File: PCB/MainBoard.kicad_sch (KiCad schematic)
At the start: 34 parts, among them J1 DM3AT-SF-PEJM5, J3 PROG, J5 Conn_01x03, J5 Conn_01x07, SW1 SW_Push, SW2 SW_Push, SW3 SW_Push, U1 ESP32-WROOM-32D, U3 MPU-6050, U8 GY-521

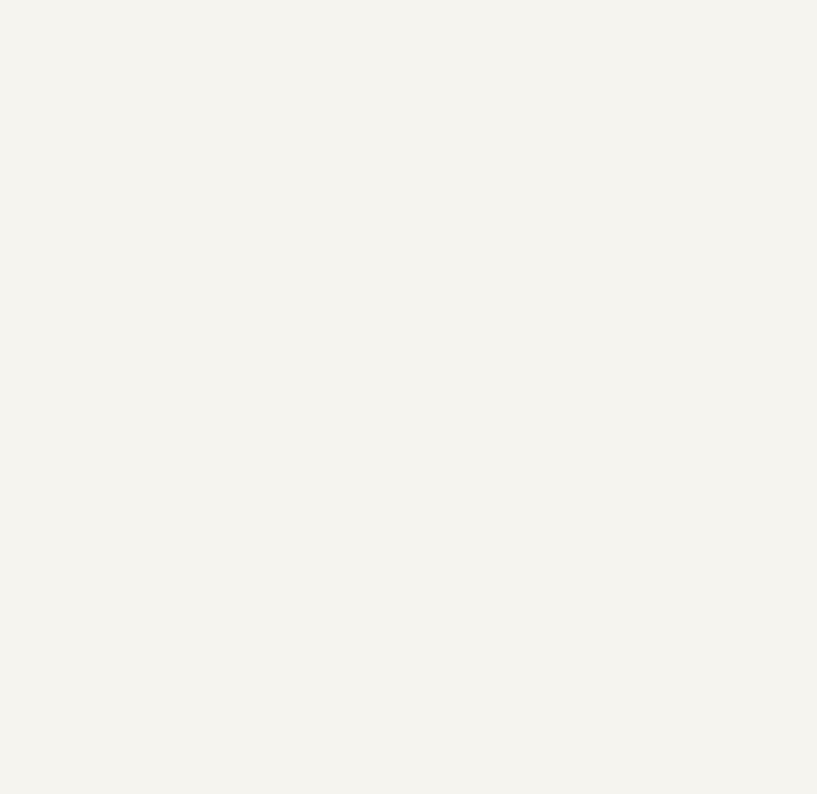
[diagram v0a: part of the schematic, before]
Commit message: Added RTC circuit
Signed-off-by: theloukou
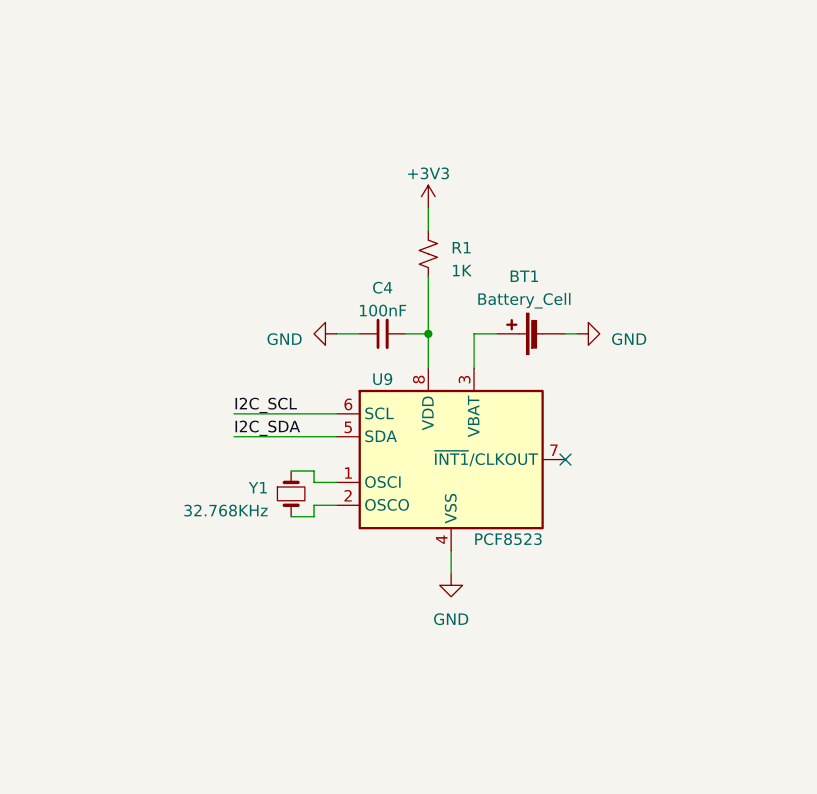
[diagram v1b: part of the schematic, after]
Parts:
- added BT1: Battery_Cell, Battery:BatteryHolder_Keystone_3000_1x12mm, symbol Device:Battery_Cell
- added C4: 100nF, Capacitor_SMD:C_0603_1608Metric, symbol Device:C_Small
- added R1: 1K, Resistor_SMD:R_0603_1608Metric, symbol Device:R_Small_US
- added U9: PCF8523, Package_SO:SOIC-8_3.9x4.9mm_P1.27mm, symbol Timer_RTC:PCF8523T
- added Y1: 32.768KHz, Crystal:Crystal_C38-LF_D3.0mm_L8.0mm_Horizontal, symbol Device:Crystal_Small
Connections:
- net +3V3: now also R1.1
- net GND: now also BT1.2 (-), C4.1, U9.4 (VSS)
- net I2C_SCL: now also U9.6 (SCL)
- net I2C_SDA: now also U9.5 (SDA)
- new net: C4.2, R1.2, U9.8 (VDD)
- new net: U9.1 (OSCI), Y1.1
- new net: U9.2 (OSCO), Y1.2
- new net: BT1.1 (+), U9.3 (VBAT)
- no-connect marks 19 -> 20

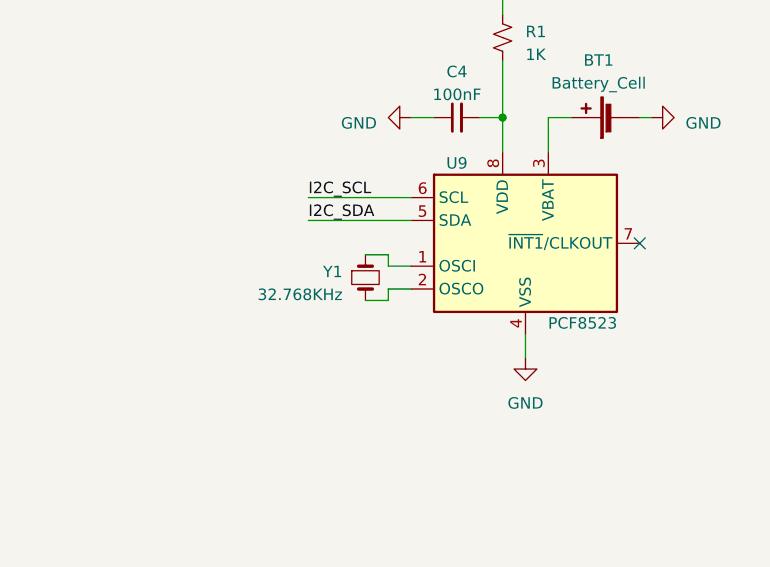
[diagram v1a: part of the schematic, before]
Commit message: Finalized RTC layout changes
Signed-off-by: theloukou
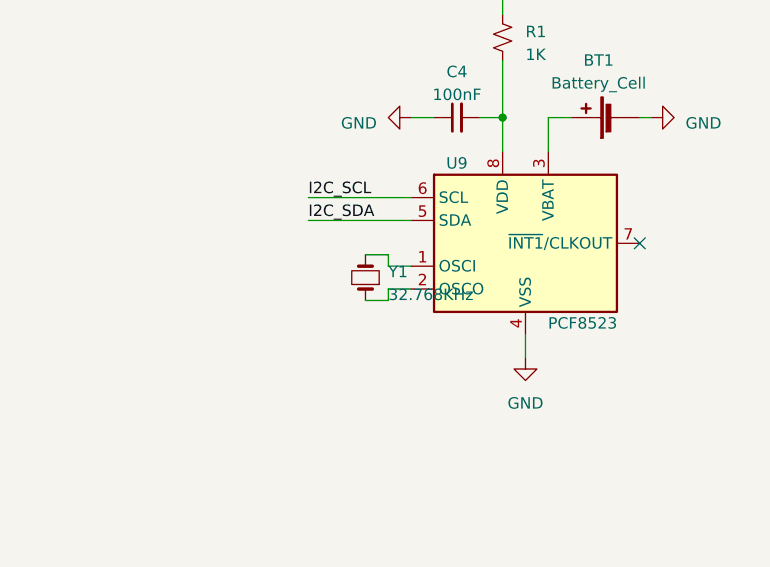
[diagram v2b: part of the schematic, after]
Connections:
- net at Y1.1: now also U9.2 (OSCO); no longer U9.1 (OSCI)
- net at Y1.2: now also U9.1 (OSCI); no longer U9.2 (OSCO)
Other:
- moved on the sheet: Y1
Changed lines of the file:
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@@
     )
   )
-  (symbol (lib_id "Device:Crystal_Small") (at 64.77 171.45 270) (unit 1)
+  (symbol (lib_id "Device:Crystal_Small") (at 64.77 171.45 90) (unit 1)
     (in_bom yes) (on_board yes) (dnp no) (fields_autoplaced)
-    (property "Reference" "Y1" (at 62.23 170.815 90)
+    (property "Reference" "Y1" (at 67.31 170.815 90)
       (effects (font (size 1.27 1.27)) (justify right))
     )
-    (property "Value" "32.768KHz" (at 62.23 173.355 90)
+    (property "Value" "32.768KHz" (at 67.31 173.355 90)
       (effects (font (size 1.27 1.27)) (justify right))
     )

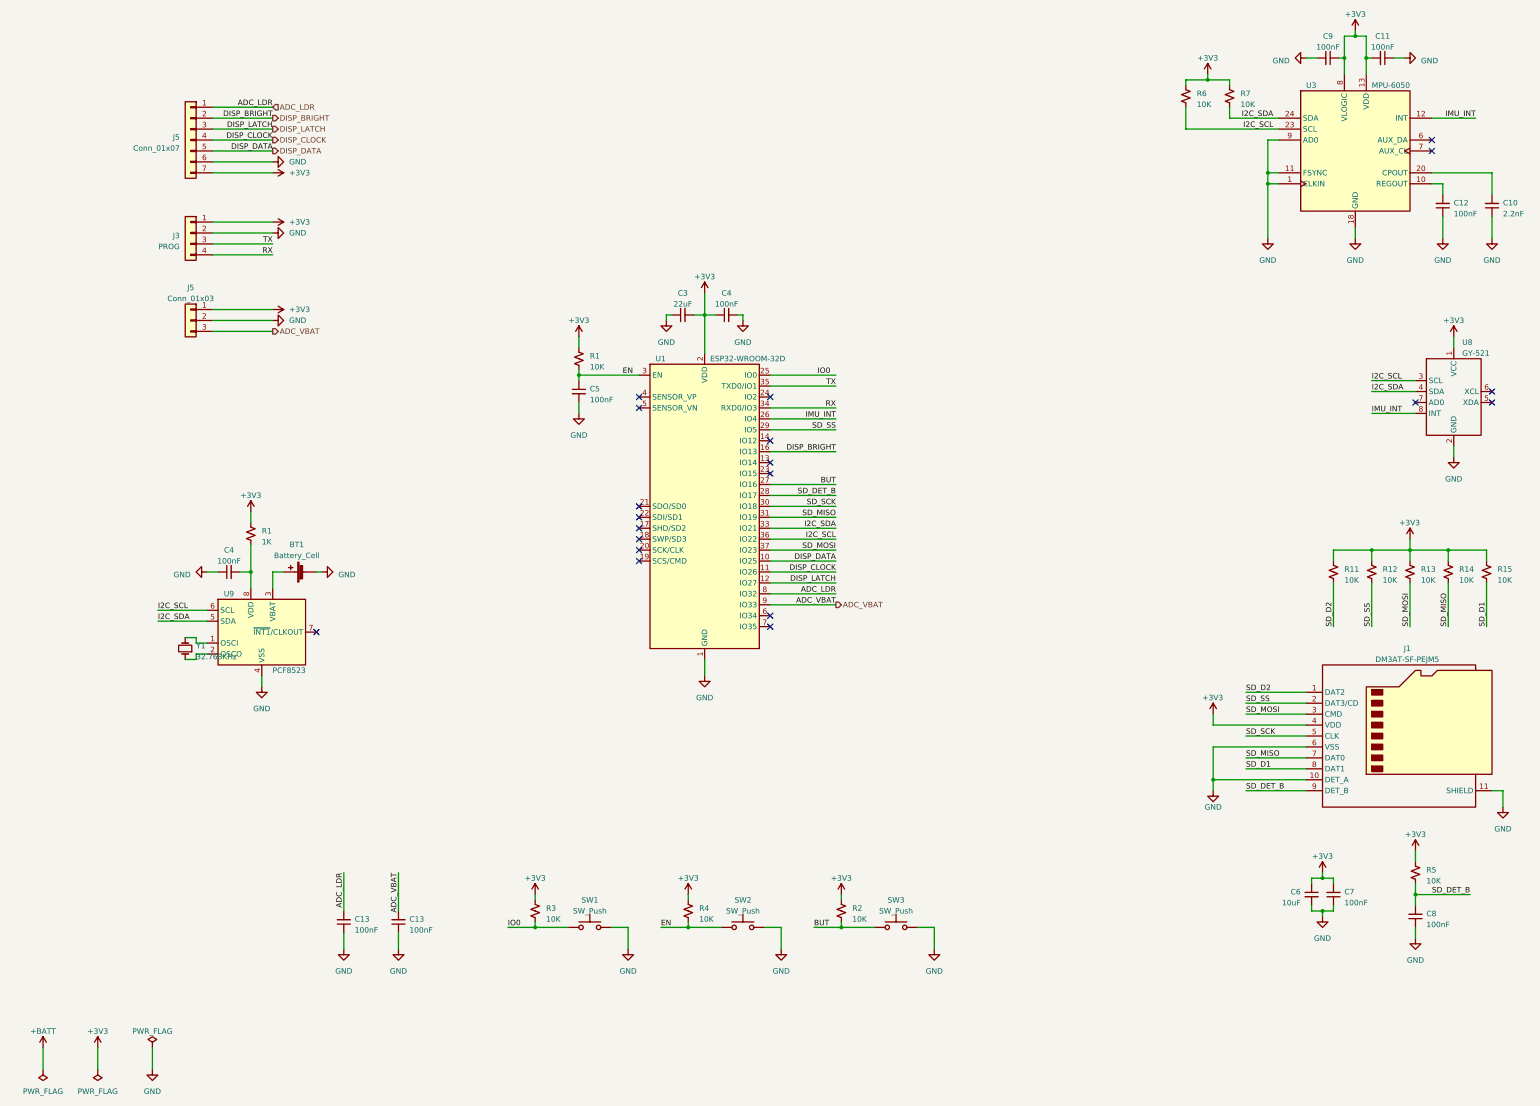
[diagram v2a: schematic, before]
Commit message: Minor adjustments on PCB
Signed-off-by: theloukou
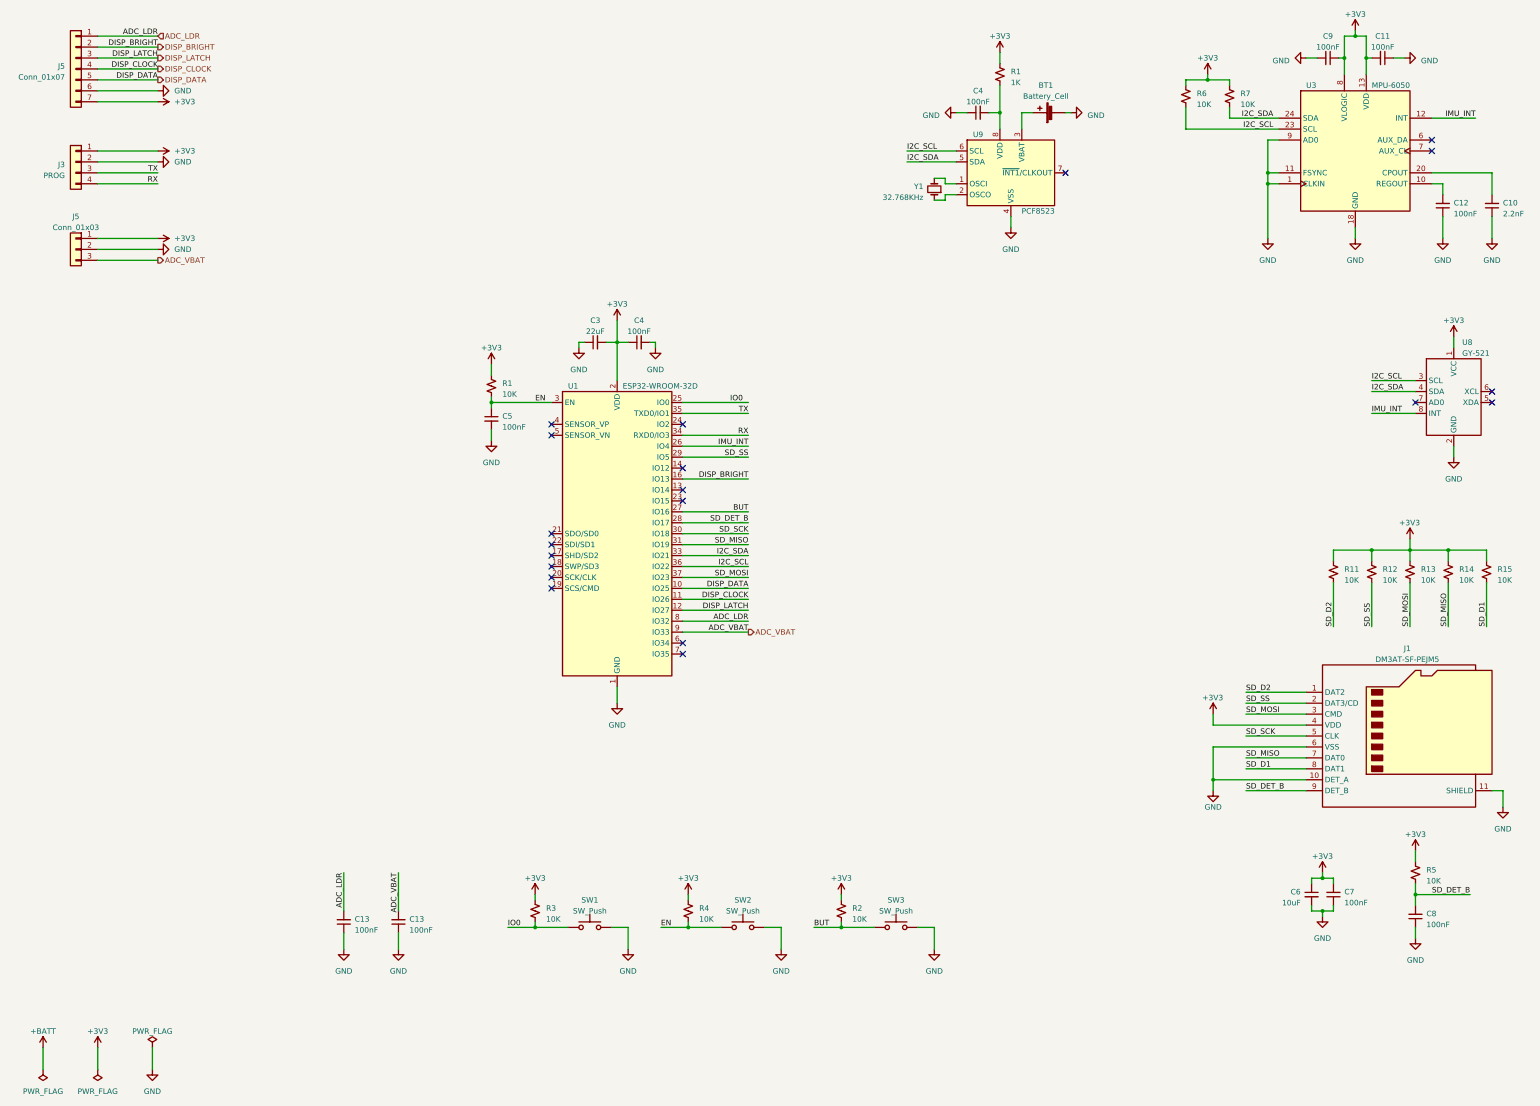
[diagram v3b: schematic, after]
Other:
- moved on the sheet: BT1, C3, C4, C5, J3, J5, R1, U1, U9, Y1
